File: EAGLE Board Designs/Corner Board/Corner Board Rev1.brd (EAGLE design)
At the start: 100 x 50 mm, 19 parts, among them J1 CONNECTOR-4_μF_T_V_BLACK, J2 CONNECTOR-2_MOLEX_NANOFIT_PTH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, J3 CONNECTOR-10_MF_T_V_, J4 CONNECTOR-4_μF_T_V_BLACK, J5 CONNECTOR-4_μF_T_V_BLACK, U1 VOLTAGE_REGULATOR_SOT-89_15V, U2 OPAMP_1_CHANNEL_OPA991, U3 INA823DT

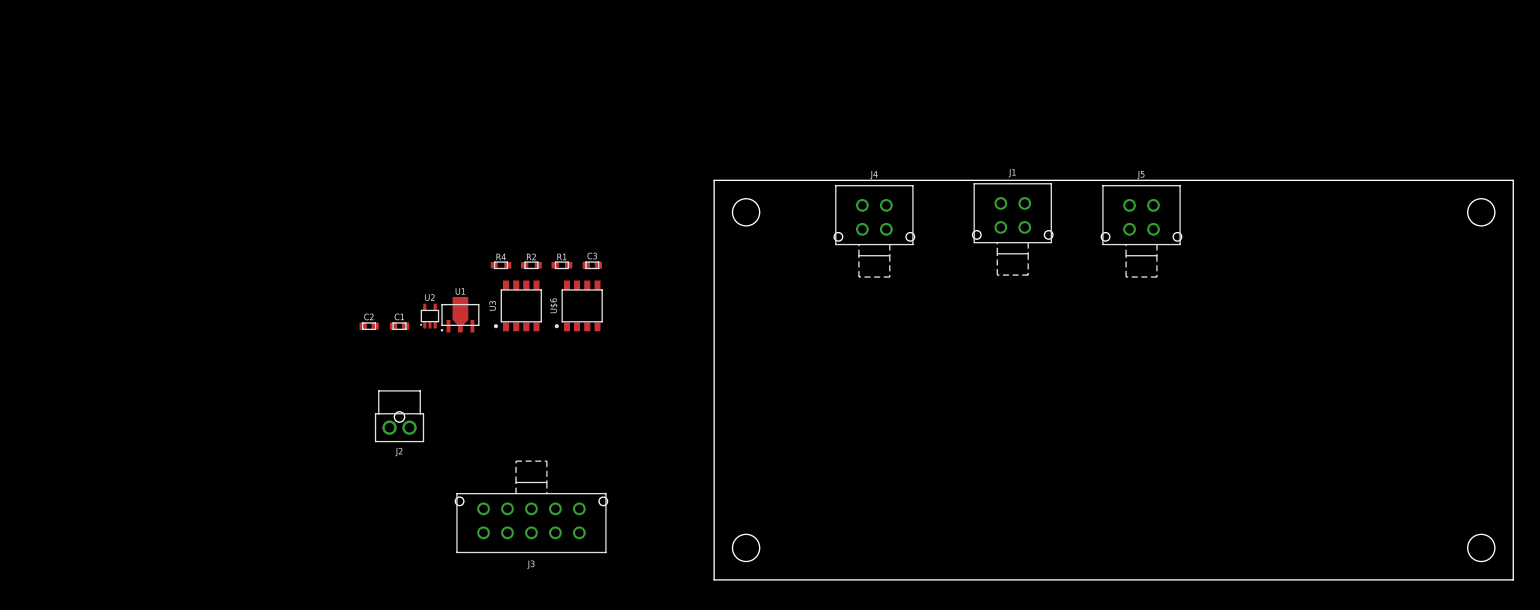
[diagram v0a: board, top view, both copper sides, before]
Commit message: updated to amphenol connectors
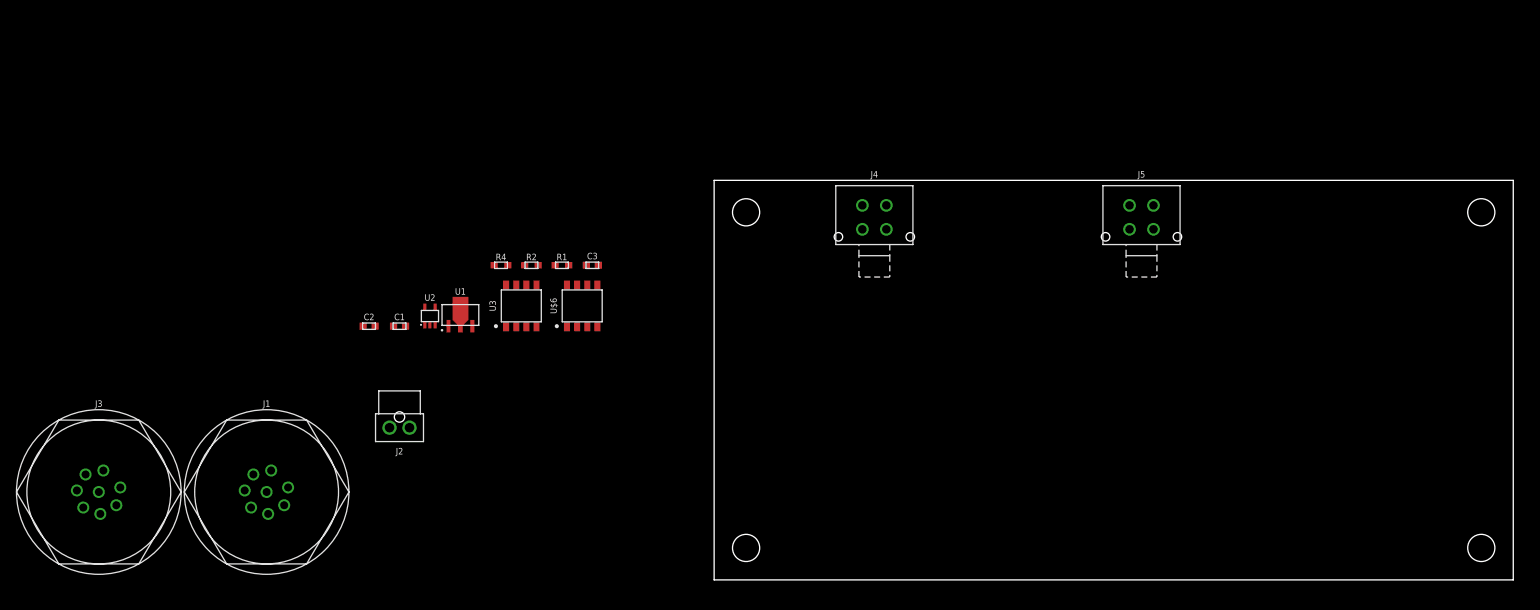
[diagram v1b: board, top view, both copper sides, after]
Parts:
- J1: value CONNECTOR-4_μF_T_V_BLACK -> CONNECTOR-8_AMPHENOL_M12A_08PMMP_; device HyTechDevices:MOLEX_MICROFIT_PTH_VERTICAL_04_DUAL -> HyTechDevices:M12A-08PMMP
- J3: value CONNECTOR-10_MF_T_V_ -> CONNECTOR-8_AMPHENOL_M12A_08PMMP_; device HyTechDevices:MOLEX_MICROFIT_PTH_VERTICAL_10_DUAL -> HyTechDevices:M12A-08PMMP
- moved J1 99.1 mm to (-56.0, 11.0), turned to 0 degrees
- moved J3 54.2 mm to (-77.0, 11.0)
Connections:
- removed net OUT: C3.1, U$6.6
- net +24V: now also J1.1; no longer J3.1
- net 10V: now also C3.1, J3.1, U$6.6; no longer J1.1
- net GND: now also J1.8, J3.8; no longer J1.4, J3.10
- net LOAD_CELL_AMPLIFIED: now also J1.2; no longer J3.2
- net POSTINTERLOCK: now also J1.6; no longer J3.6
- net PREINTERLOCK: now also J1.5; no longer J3.5
- net SIGNAL+: now also J3.4; no longer J1.2
- net SIGNAL-: now also J3.5; no longer J1.3
- net SUS_POT_1: now also J1.3; no longer J3.3
- net SUS_POT_2: now also J1.4; no longer J3.4

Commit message: preliminary placement of parts will change later
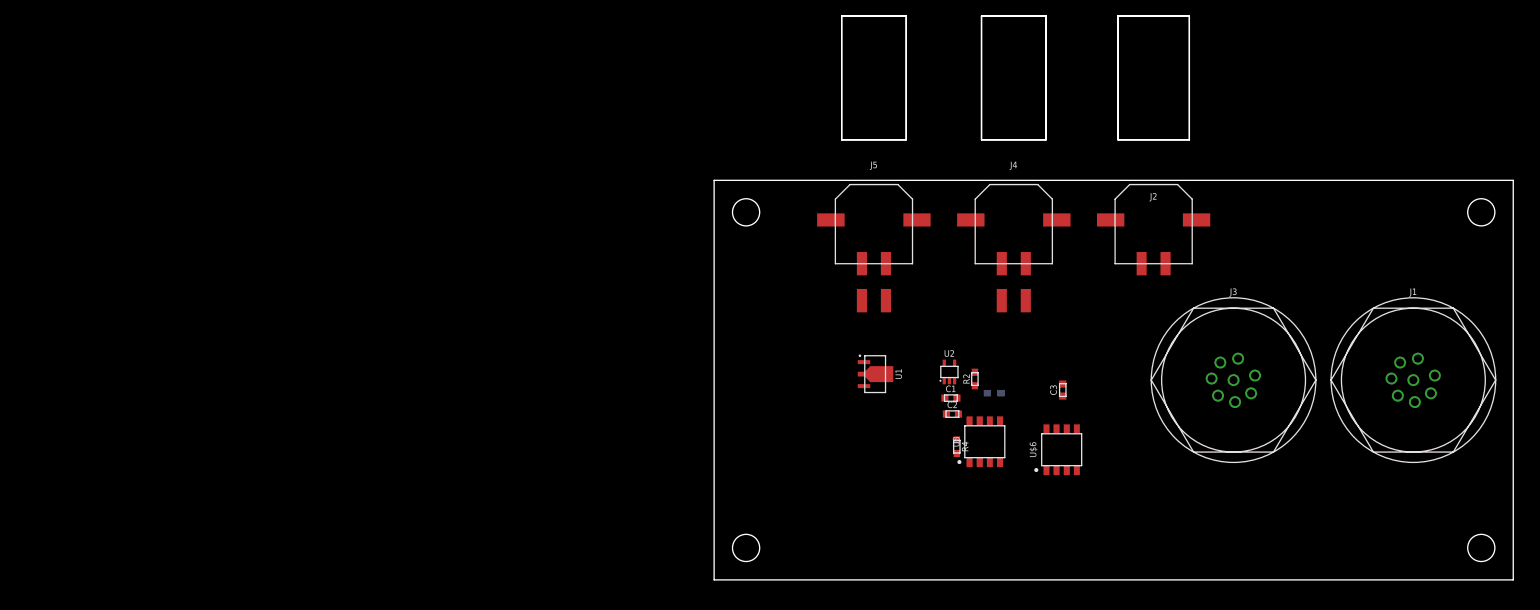
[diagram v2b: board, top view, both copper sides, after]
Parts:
- J2: value CONNECTOR-2_MOLEX_NANOFIT_PTH_VERTICAL_02_BLACK -> CONNECTOR-2_MICROFIT_SMD_RIGHTANGLE_02_SINGLE_BLACK; device HyTechDevices:MOLEX_NANOFIT_PTH_02 -> HyTechDevices:MOLEX_MICROFIT_SMD_RIGHTANGLE_02_SINGLE
- J4, J5: value CONNECTOR-4_μF_T_V_BLACK -> CONNECTOR-4_μF_S_RA_; device HyTechDevices:MOLEX_MICROFIT_PTH_VERTICAL_04_DUAL -> HyTechDevices:MOLEX_MICROFIT_SMD_RIGHTANGLE_04_DUAL
- moved J1 144.2 mm to (87.5, 25.0)
- moved J3 142.7 mm to (65.0, 25.0)
- moved J2 97.9 mm to (55.0, 45.0), turned to 180 degrees
- moved C2 73.8 mm to (29.8, 20.8)
- moved C1 69.6 mm to (29.6, 22.8)
- moved U2 65.4 mm to (29.4, 26.0)
- moved U$6 62.6 mm to (43.5, 16.3)
- moved R4 61.4 mm to (30.4, 16.7), turned to 270 degrees
- moved C3 60.9 mm to (43.6, 23.8), turned to 90 degrees
- moved U3 60.4 mm to (33.9, 17.3)
- moved R2 57.3 mm to (32.6, 25.1), turned to 90 degrees
- moved R1 56.4 mm to (35.0, 23.4), flipped to the bottom
- moved U1 50.9 mm to (18.8, 25.8), turned to 270 degrees
- moved J5 33.5 mm to (20.0, 45.0)
- moved J4 17.5 mm to (37.5, 45.0)

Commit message: some edits
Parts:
- added C4, C5: CAPACITOR_0603_25V_0.1UF, HyTechDevices:0603-CAP
- added R3, R7: RESISTOR_0603_10K, HyTechDevices:0603-RES
- added R5, R8: RESISTOR_0603_2.74K, HyTechDevices:0603-RES
- added R6, R9: RESISTOR_0603_10.5K, HyTechDevices:0603-RES
- added U4, U5: OPAMP_1_CHANNEL_OPA991, HyTechDevices:SC-70-5
- R4: value RESISTOR_0603_50 -> RESISTOR_0603_2.74K
- moved C2 0.71 mm to (29.3, 20.2)
- moved R4 0.50 mm to (29.9, 16.7)
- flipped R1 to the top
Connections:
- new net N$5: R5.2, R6.1, U4.3
- new net N$7: R7.1, R8.1
- new net N$8: R8.2, R9.1, U5.3
- new net SUS_POT_1_24V: J1.3, R9.2, U5.4
- new net SUS_POT_2_24V: J1.4, R6.2, U4.4
- net +24V: now also C4.1, C5.1, U4.5, U5.5
- net GND: now also C4.2, C5.2, R3.1, R5.1, U4.2, U5.2
- net SUS_POT_1: now also R7.2, U5.1; no longer J1.3
- net SUS_POT_2: now also R3.2, U4.1; no longer J1.4
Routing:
- net +24V: track 0.00 -> 5.49 mm

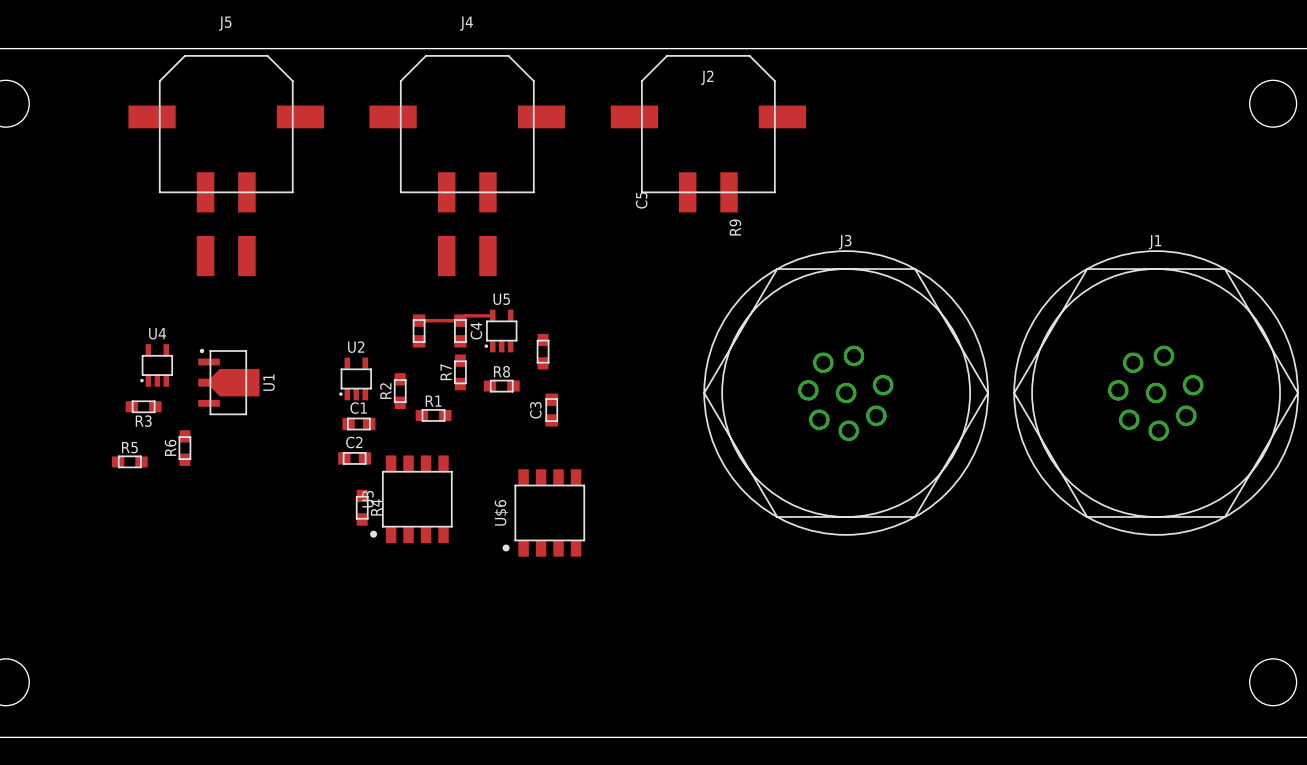
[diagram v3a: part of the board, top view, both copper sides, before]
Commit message: finnished routing
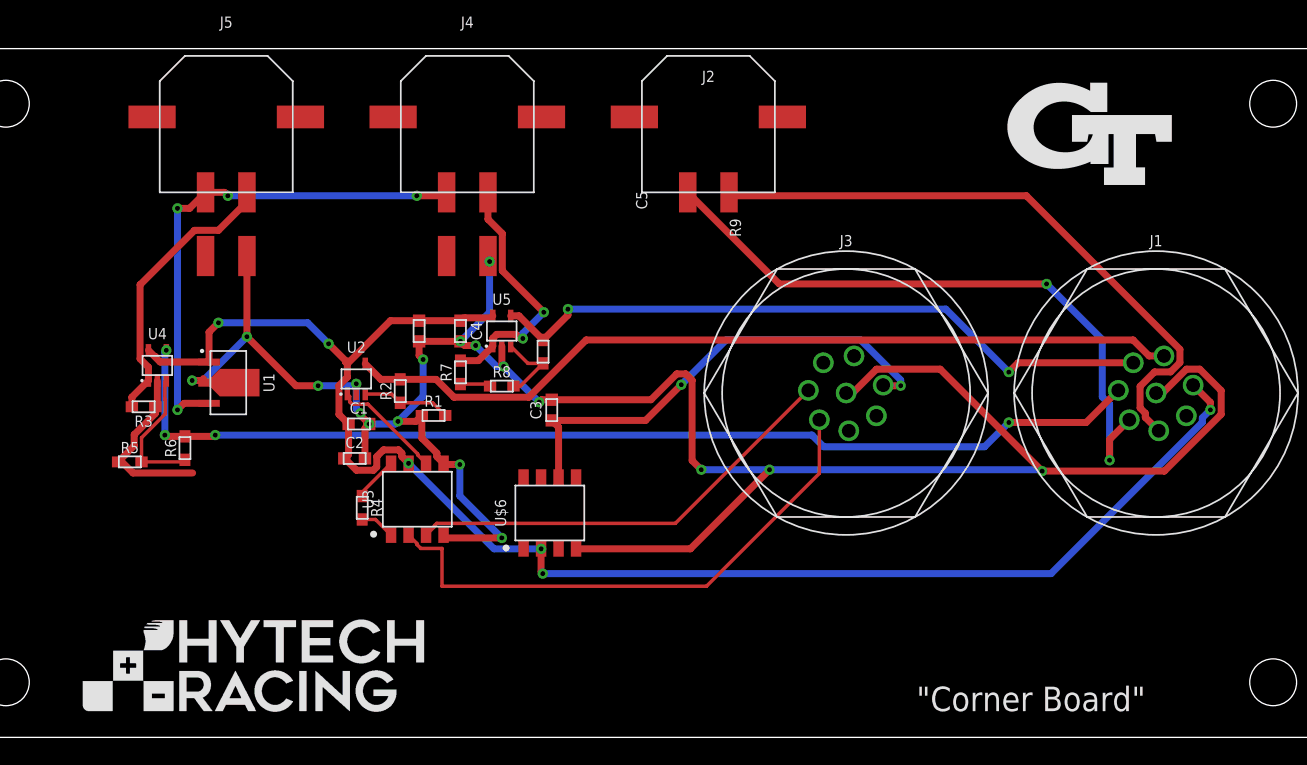
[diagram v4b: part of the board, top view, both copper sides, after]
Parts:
- added U$13: (no value), HyTechManufacturing:LOGO_HYTECH_MEDIUM
- added U$14: (no value), HyTechManufacturing:LOGO_GT_MEDIUM
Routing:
- net GND: track 0.00 -> 187.0 mm, vias 0 -> 18
- net +24V: track 5.49 -> 114.9 mm, vias 0 -> 6
- net SUS_POT_2_24V: track 0.00 -> 77.5 mm, vias 0 -> 4
- net LOAD_CELL_AMPLIFIED: track 0.00 -> 61.2 mm
- net SUS_POT_1_24V: track 0.00 -> 49.3 mm, vias 0 -> 2
- net PREINTERLOCK: track 0.00 -> 47.0 mm, vias 0 -> 2
- net POSTINTERLOCK: track 0.00 -> 45.5 mm
- net SIGNAL-: track 0.00 -> 40.3 mm
- net 15V: track 0.00 -> 37.3 mm, vias 0 -> 4
- net 10V: track 0.00 -> 35.0 mm, vias 0 -> 2
- net SIGNAL+: track 0.00 -> 32.1 mm
- net SUS_POT_2: track 0.00 -> 19.2 mm
- net SUS_POT_1: track 0.00 -> 18.7 mm, vias 0 -> 2
- net N$5: track 0.00 -> 9.89 mm
- net N$3: track 0.00 -> 8.07 mm
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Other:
- board text added: ""Corner Board""

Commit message: ratsnest
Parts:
- moved U4 21.5 mm to (33.7, 16.3)
- moved R4 17.4 mm to (12.7, 19.3)
- moved R5 16.4 mm to (28.6, 15.0)
- moved U3 16.2 mm to (17.9, 20.0)
- moved R3 16.2 mm to (28.7, 17.1), turned to 0 degrees
- moved C5 13.3 mm to (37.0, 16.5)
- moved R6 11.7 mm to (28.6, 19.6), turned to 0 degrees
- moved R1 10.7 mm to (25.5, 28.3)
- moved R7 10.0 mm to (46.8, 24.6), turned to 270 degrees
- moved R9 8.39 mm to (51.4, 27.6)
- moved C3 8.15 mm to (48.2, 17.0), turned to 270 degrees
- moved C2 7.05 mm to (22.4, 21.7), turned to 90 degrees
- moved U5 6.25 mm to (43.8, 24.5)
- moved C4 6.05 mm to (40.8, 24.8)
- moved R8 5.39 mm to (43.8, 29.3)
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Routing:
- net GND: track 187.0 -> 0.00 mm, vias 18 -> 0
- net +24V: track 114.9 -> 0.00 mm, vias 6 -> 0
- net SUS_POT_2_24V: track 77.5 -> 0.00 mm, vias 4 -> 0
- net LOAD_CELL_AMPLIFIED: track 61.2 -> 0.00 mm
- net SUS_POT_1_24V: track 49.3 -> 0.00 mm, vias 2 -> 0
- net PREINTERLOCK: track 47.0 -> 0.00 mm, vias 2 -> 0
- net POSTINTERLOCK: track 45.5 -> 0.00 mm
- net SIGNAL-: track 40.3 -> 0.00 mm
- net 15V: track 37.3 -> 0.00 mm, vias 4 -> 0
- net 10V: track 35.0 -> 0.00 mm, vias 2 -> 0
- net SIGNAL+: track 32.1 -> 0.00 mm
- net SUS_POT_2: track 19.2 -> 0.00 mm
- net SUS_POT_1: track 18.7 -> 0.00 mm, vias 2 -> 0
- net N$5: track 9.89 -> 0.00 mm
- net N$3: track 8.07 -> 0.00 mm
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- added copper zone on layer 16, net +24V
- added copper zone on layer 1, net GND

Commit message: Finished routing.
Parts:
- moved R1 0.18 mm to (25.4, 28.4)
- moved R8 0.16 mm to (43.7, 29.2)
- moved U5 0.15 mm to (43.7, 24.6)
- moved U3 0.14 mm to (17.8, 20.1)
- moved U4 0.14 mm to (33.8, 16.3)
- moved C2 0.13 mm to (22.4, 21.6)
- moved R3 0.13 mm to (28.7, 17.3)
- moved C4 0.12 mm to (40.9, 24.9)
- moved R7 0.12 mm to (46.7, 24.6)
- moved U$6 0.11 mm to (44.2, 17.5)
- moved R5 0.10 mm to (28.7, 15.0)
- moved R9 0.10 mm to (51.3, 27.7), turned to 270 degrees
- moved U1 0.09 mm to (16.0, 28.7)
- moved R6 0.08 mm to (28.7, 19.6)
- moved C3 0.07 mm to (48.3, 17.0)
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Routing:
- net SUS_POT_2_24V: track 0.00 -> 64.3 mm, vias 0 -> 2
- net LOAD_CELL_AMPLIFIED: track 0.00 -> 63.4 mm, vias 0 -> 2
- net SIGNAL-: track 0.00 -> 54.5 mm
- net SIGNAL+: track 0.00 -> 50.0 mm
- net SUS_POT_1_24V: track 0.00 -> 47.9 mm, vias 0 -> 2
- net SUS_POT_2: track 0.00 -> 41.2 mm, vias 0 -> 2
- net PREINTERLOCK: track 0.00 -> 40.5 mm
- net POSTINTERLOCK: track 0.00 -> 39.5 mm
- net 10V: track 0.00 -> 30.8 mm
- net 15V: track 0.00 -> 30.1 mm
- net SUS_POT_1: track 0.00 -> 28.5 mm
- net N$3: track 0.00 -> 16.9 mm
- net +24V: track 0.00 -> 15.8 mm, vias 0 -> 9
- net N$8: track 0.00 -> 14.6 mm, vias 0 -> 2
- net N$5: track 0.00 -> 11.7 mm
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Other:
- board text added: "Corner Board Shayan Noorani Liwei Sun"
- board text removed: ""Corner Board""

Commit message: design review changes
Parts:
- renumbered U$6 to U6

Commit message: design review changes
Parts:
- R2: value RESISTOR_0603_10K -> RESISTOR_0603_22.1K
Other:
- board text added: "Corner Board rev1 Designed by: Liwei Sun Shayan Noorani"
- board text removed: "Corner Board Shayan Noorani Liwei Sun"
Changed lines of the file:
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@@
 <wire x1="100" y1="50" x2="0" y2="50" width="0" layer="20"/>
 <wire x1="0" y1="50" x2="0" y2="0" width="0" layer="20"/>
-<text x="70.104" y="1.905" size="1.778" layer="25">Corner Board
-Shayan Noorani
-Liwei Sun</text>
+<text x="74.168" y="3.048" size="1.27" layer="21" font="vector">Corner Board rev1
+Designed by:
+Liwei Sun
+Shayan Noorani</text>
 </plain>
 <attributes>
@@
 <attribute name="VOLTAGE_MAX" value="50V" x="44.45" y="-10.922" size="1.778" layer="27" display="off"/>
 </element>
-<element name="R2" library="HyTechDevices" package="0603-RES" value="RESISTOR_0603_10K" x="28.702" y="27.178" smashed="yes" rot="R90">
-<attribute name="DKPN" value="311-10.0KHRCT-ND" x="68.072" y="50.038" size="1.778" layer="27" rot="R90" display="off"/>
-<attribute name="MANUFACTURER" value="Yageo" x="68.072" y="50.038" size="1.778" layer="27" rot="R90" display="off"/>
-<attribute name="MOPN" value="603-RC0603FR-0710KL" x="68.072" y="50.038" size="1.778" layer="27" rot="R90" display="off"/>
-<attribute name="MPN" value="RC0603FR-0710KL" x="68.072" y="50.038" size="1.778" layer="27" rot="R90" display="off"/>
+<element name="R2" library="HyTechDevices" package="0603-RES" value="RESISTOR_0603_22.1K" x="28.702" y="27.178" smashed="yes" rot="R90">
+<attribute name="DKPN" value="P22.1KDBCT-ND" x="68.072" y="50.038" size="1.778" layer="27" rot="R90" display="off"/>
+<attribute name="MANUFACTURER" value="Panasonic Electronic Components" x="68.072" y="50.038" size="1.778" layer="27" rot="R90" display="off"/>
+<attribute name="MOPN" value="667-ERA-3AEB2212V" x="68.072" y="50.038" size="1.778" layer="27" rot="R90" display="off"/>
+<attribute name="MPN" value="ERA-3AEB2212V" x="68.072" y="50.038" size="1.778" layer="27" rot="R90" display="off"/>
 <attribute name="NAME" x="27.686" y="27.178" size="0.8128" layer="25" font="vector" rot="R90" align="bottom-center"/>
 <attribute name="POWER" value="0.1W" x="68.072" y="50.038" size="1.778" layer="27" rot="R90" display="off"/>
-<attribute name="RESISTANCE" value="10k" x="68.072" y="50.038" size="1.778" layer="27" rot="R90" display="off"/>
-<attribute name="TOLERANCE" value="1%" x="68.072" y="50.038" size="1.778" layer="27" rot="R90" display="off"/>
-<attribute name="VOLTAGE_CONTINUOUS" value="31.62V" x="68.072" y="50.038" size="1.778" layer="27" rot="R90" display="off"/>
+<attribute name="RESISTANCE" value="22.1k" x="68.072" y="50.038" size="1.778" layer="27" rot="R90" display="off"/>
+<attribute name="TOLERANCE" value="0.1%" x="68.072" y="50.038" size="1.778" layer="27" rot="R90" display="off"/>
+<attribute name="VOLTAGE_CONTINUOUS" value="47.01V" x="68.072" y="50.038" size="1.778" layer="27" rot="R90" display="off"/>
 <attribute name="VOLTAGE_MAX" value="75V" x="68.072" y="50.038" size="1.778" layer="27" rot="R90" display="off"/>
 </element>
@@
 <contactref element="J5" pad="4"/>
 <contactref element="U1" pad="2"/>
-<contactref element="R1" pad="1"/>
-<contactref element="U3" pad="5"/>
 <contactref element="C1" pad="2"/>
 <contactref element="U2" pad="2"/>
@@
 <vertex x="100.584" y="50.546"/>
 </polygon>
+<contactref element="R1" pad="1"/>
+<contactref element="U3" pad="5"/>
 </signal>
 <signal name="SIGNAL+">
@@
 <contactref element="J2" pad="1"/>
 <contactref element="J1" pad="5"/>
-<wire x1="53.5014" y1="39.5663" x2="55.8451" y2="41.91" width="0.254" layer="1"/>
-<wire x1="55.8451" y1="41.91" x2="57.658" y2="41.91" width="0.254" layer="1"/>
+<wire x1="55.0831" y1="41.91" x2="53.5014" y2="40.3283" width="0.254" layer="1"/>
+<wire x1="53.5014" y1="39.5663" x2="53.5014" y2="40.3283" width="0.254" layer="1"/>
+<wire x1="55.0831" y1="41.91" x2="57.658" y2="41.91" width="0.254" layer="1"/>
 <wire x1="57.658" y1="41.91" x2="78.486" y2="21.082" width="0.254" layer="1"/>
 <wire x1="78.486" y1="21.082" x2="84.344" y2="21.082" width="0.254" layer="1"/>
@@
 <signal name="LOAD_CELL_AMPLIFIED">
 <contactref element="U2" pad="4"/>
-<contactref element="R2" pad="2"/>
 <contactref element="J1" pad="2"/>
 <wire x1="32.484" y1="30.48" x2="30.48" y2="30.48" width="0.254" layer="1"/>
-<wire x1="30.48" y1="30.48" x2="28.702" y2="28.702" width="0.254" layer="1"/>
-<wire x1="28.702" y1="28.702" x2="28.702" y2="28.028" width="0.254" layer="1"/>
+<wire x1="28.702" y1="28.702" x2="30.48" y2="30.48" width="0.254" layer="1"/>
 <wire x1="34.686" y1="28.278" x2="32.484" y2="30.48" width="0.254" layer="1"/>
 <wire x1="34.686" y1="28.278" x2="35.56" y2="29.152" width="0.254" layer="1"/>
@@
 <wire x1="82.2336625" y1="30.48" x2="86.92875625" y2="25.78490625" width="0.254" layer="1"/>
 <wire x1="36.83" y1="30.48" x2="75.692" y2="30.48" width="0.254" layer="16"/>
+<contactref element="R2" pad="2"/>
+<wire x1="28.702" y1="28.028" x2="28.702" y2="28.702" width="0.254" layer="1"/>
 </signal>
 <signal name="SUS_POT_1_24V">
